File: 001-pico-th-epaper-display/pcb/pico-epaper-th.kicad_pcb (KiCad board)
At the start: 2 copper layers, 70 x 70 mm, 17 parts, among them Q1 AO3407, U1 GY-SHT31-D, U2 TPL5110, U3 WS_1_54_epaper_module

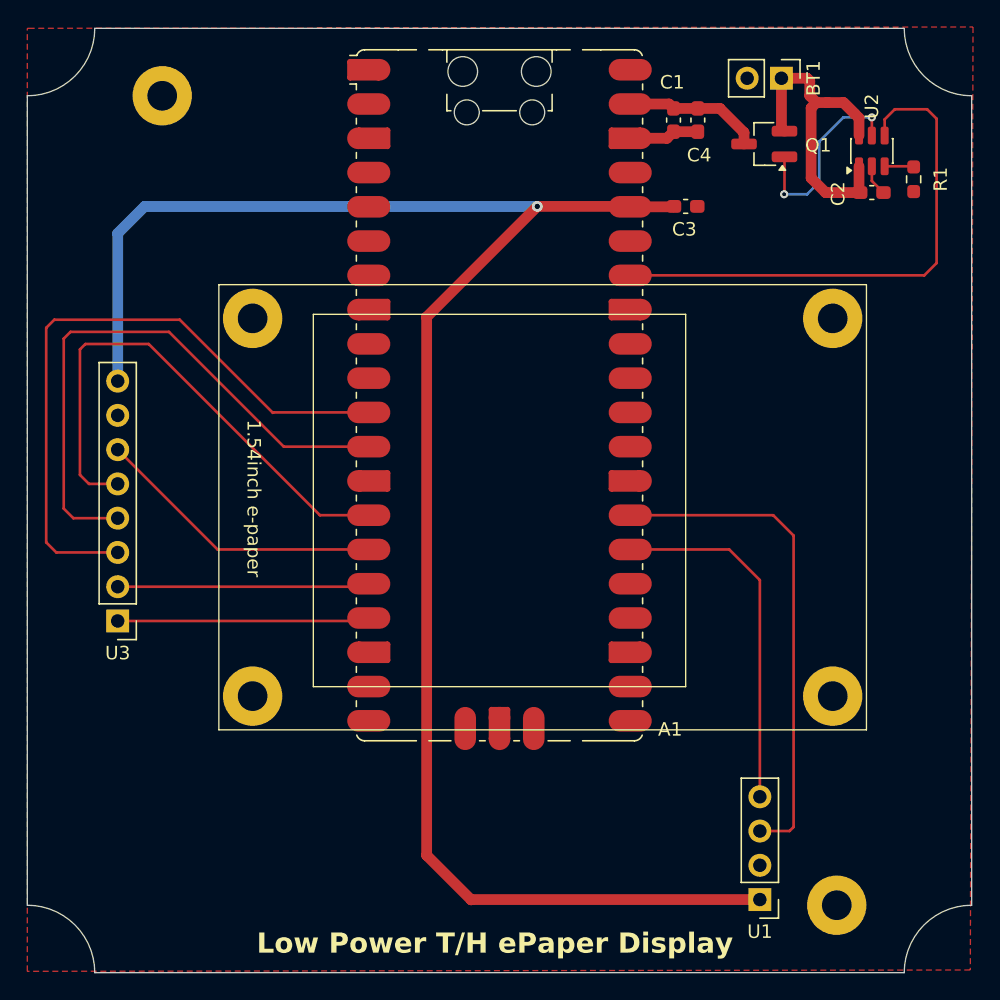
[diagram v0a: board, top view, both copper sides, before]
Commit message: fixed drc errors on pcb
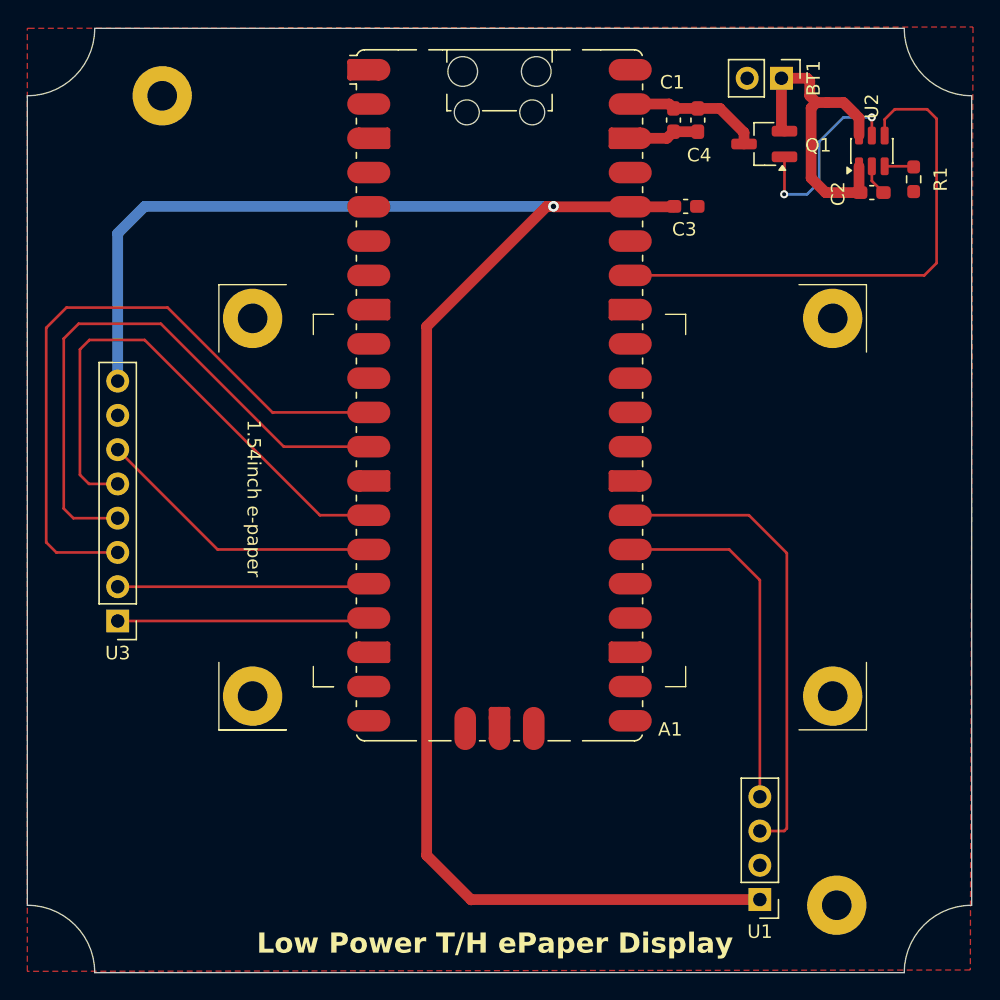
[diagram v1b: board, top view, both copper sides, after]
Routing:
- net Net-(A1-GPIO21): track 37.0 -> 35.3 mm
- net /3V3: track 130.6 -> 131.4 mm
- net Net-(A1-GPIO8): track 48.5 -> 49.3 mm

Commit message: updated pcb
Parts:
- moved REF** 0.50 mm to (117.1, 121.3)
- moved REF** 0.50 mm to (117.1, 93.3)
- moved REF** 0.50 mm to (160.1, 93.3)
- moved REF** 0.50 mm to (160.1, 121.3)
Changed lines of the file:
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@@
 	(footprint "MountingHole:MountingHole_2.2mm_M2_Pad"
 		(layer "F.Cu")
-		(at 117.1 121.8)
+		(at 117.1 121.3)
 		(descr "Mounting Hole 2.2mm, M2, generated by kicad-footprint-generator mountinghole.py")
 		(tags "mountinghole M2")
@@
 	(footprint "MountingHole:MountingHole_2.2mm_M2_Pad"
 		(layer "F.Cu")
-		(at 117.1 93.8)
+		(at 117.1 93.3)
 		(descr "Mounting Hole 2.2mm, M2, generated by kicad-footprint-generator mountinghole.py")
 		(tags "mountinghole M2")
@@
 	(footprint "MountingHole:MountingHole_2.2mm_M2_Pad"
 		(layer "F.Cu")
-		(at 160.1 93.8)
+		(at 160.1 93.3)
 		(descr "Mounting Hole 2.2mm, M2, generated by kicad-footprint-generator mountinghole.py")
 		(tags "mountinghole M2")
@@
 	(footprint "MountingHole:MountingHole_2.2mm_M2_Pad"
 		(layer "F.Cu")
-		(at 160.1 121.8)
+		(at 160.1 121.3)
 		(descr "Mounting Hole 2.2mm, M2, generated by kicad-footprint-generator mountinghole.py")
 		(tags "mountinghole M2")
@@
 	)
 	(gr_line
-		(start 114.6 91.3)
-		(end 114.6 96.3)
+		(start 114.6 90.8)
+		(end 114.6 95.8)
 		(stroke
 			(width 0.1)
@@
 	)
 	(gr_line
-		(start 114.6 91.3)
-		(end 119.6 91.3)
+		(start 114.6 90.8)
+		(end 119.6 90.8)
 		(stroke
 			(width 0.1)
@@
 	)
 	(gr_line
-		(start 114.6 124.3)
-		(end 114.6 119.3)
+		(start 114.6 123.8)
+		(end 114.6 118.8)
 		(stroke
 			(width 0.1)
@@
 	)
 	(gr_line
-		(start 114.6 124.3)
-		(end 119.6 124.3)
+		(start 119.6 123.8)
+		(end 114.6 123.8)
 		(stroke
 			(width 0.1)
@@
 	)
 	(gr_line
-		(start 119.6 124.3)
-		(end 114.6 124.3)
-		(stroke
-			(width 0.1)
-			(type default)
-		)
-		(layer "F.SilkS")
-	)
-	(gr_line
-		(start 121.6 93.5)
-		(end 121.6 95)
+		(start 121.6 93)
+		(end 121.6 94.5)
 		(stroke
 			(width 0.1)
@@
 	)
 	(gr_line
-		(start 121.6 121.1)
-		(end 121.6 119.6)
+		(start 121.6 120.6)
+		(end 121.6 119.1)
 		(stroke
 			(width 0.1)
@@
 	)
 	(gr_line
-		(start 149.2 93.5)
-		(end 147.7 93.5)
+		(start 149.2 93)
+		(end 149.2 94.5)
 		(stroke
 			(width 0.1)
@@
 	(gr_line
 		(start 149.2 93.5)
-		(end 149.2 95)
+		(end 147.7 93.5)
 		(stroke
 			(width 0.1)
@@
 	)
 	(gr_line
-		(start 149.2 121.1)
-		(end 147.7 121.1)
+		(start 149.2 120.6)
+		(end 149.2 119.1)
 		(stroke
 			(width 0.1)
@@
 	(gr_line
 		(start 149.2 121.1)
-		(end 149.2 119.6)
+		(end 147.7 121.1)
 		(stroke
 			(width 0.1)
@@
 	)
 	(gr_line
-		(start 162.6 91.3)
-		(end 157.6 91.3)
+		(start 162.6 90.8)
+		(end 157.6 90.8)
 		(stroke
 			(width 0.1)
@@
 	)
 	(gr_line
-		(start 162.6 91.3)
-		(end 162.6 96.3)
+		(start 162.6 90.8)
+		(end 162.6 95.8)
 		(stroke
 			(width 0.1)
@@
 	)
 	(gr_line
-		(start 162.6 124.3)
-		(end 157.6 124.3)
+		(start 162.6 123.8)
+		(end 157.6 123.8)
 		(stroke
 			(width 0.1)
@@
 	)
 	(gr_line
-		(start 162.6 124.3)
-		(end 162.6 119.3)
+		(start 162.6 123.8)
+		(end 162.6 118.8)
 		(stroke
 			(width 0.1)
@@
 		)
 	)
+	(group ""
+		(members "0b21c482-ac06-42bb-8537-ba7dc52efd52" "11d3df77-c72c-4d33-beab-5d64c931776f"
+			"2fcb8823-c92e-4fb5-955a-d4a767ed8685" "33f97fa0-1314-4f31-9f6a-78e4fa2b2029"
+			"4e2481dd-979a-431c-9b97-598f2da462ba" "5133a679-7546-4c58-9a8a-1b1aafb9ee03"
+			"6d36ccce-9f08-448f-aa25-74471985d1e0" "72b6e6cb-d420-4a97-973e-35b18286b0bf"
+			"76dde05d-d3e6-497a-8c19-8fe20f65a19b" "7b19dc21-124c-4387-a29e-79b12b6567a7"
+			"8cd6b30b-544c-4e10-9d9a-03d61fe41231" "af498251-897e-43c8-94da-fa96e98c6e45"
+			"be3397b1-463c-4bcf-b5ec-c6337bf92907" "e6a64be3-d599-470b-b3e2-bcd8436e3f5c"
+			"f147fc86-f39c-4d85-9531-b3677f1b832b" "ff5ad6ca-04e3-41eb-81ee-58c27b653d42"
+		)
+	)
+	(group ""
+		(members "31840bb4-aa1c-466c-b5c4-a56ede7e20fa")
+	)
 	(embedded_fonts no)

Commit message: removed locked silk
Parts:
- added G***: LOGO, pico-epaper-th:logo_40, B.Cu at (135.4, 101.9)

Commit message: updated
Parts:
- added G***: LOGO, pico-epaper-th:qr_15, B.Cu at (135.4, 111.5)
- moved G*** 4.00 mm to (135.4, 97.9)
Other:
- board text removed: "electronut.in"

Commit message: added ver
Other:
- board text added: "Ver 0.1"
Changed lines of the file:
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@@
 			(disableapertmacros no)
 			(usegerberextensions no)
-			(usegerberattributes yes)
+			(usegerberattributes no)
 			(usegerberadvancedattributes yes)
 			(creategerberjobfile yes)
@@
 			(outputformat 1)
 			(mirror no)
-			(drillshape 1)
+			(drillshape 0)
 			(scaleselection 1)
-			(outputdirectory "")
+			(outputdirectory "gerbers")
 		)
 	)
@@
 		)
 	)
+	(gr_text "Ver 0.1"
+		(at 168.3 102.1 90)
+		(layer "B.SilkS")
+		(effects
+			(font
+				(size 1.5 1.5)
+				(thickness 0.3)
+				(bold yes)
+			)
+			(justify left bottom mirror)
+		)
+	)
